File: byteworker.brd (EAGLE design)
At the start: 32 x 32 mm, 65 parts, among them IC1 MCP1703, IC2 TJA1043, J2 AVRSPI-61.27, Q1 BSS138, Q2 BSS138, Q3 BSS138, Q5 BSS138, Q6 FDN5618P, X1 16 MHz, X2 bus connector

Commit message: Done routing
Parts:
- removed Q6: FDN5618P, bytewerk-fet:SOT23C
- removed U$3, U$7, U$8: (no value), bytewerk-symbol:FIDUCIAL_R
- removed X2: bus connector, con-subd:F09D
- added D4: 16V, bytewerk-diode:SOD-128
- added Q4: AP2321GN-HF-3TR, bytewerk-transistor:SOT23-3
- added X3: SUBD-H9, bytewerk-con:SUBD9
- C2: value 10u/25v -> 1u/25V
- C3: value 10u/10v -> 1u/10V
- JP2: device pinhead:1X08 -> pinhead:1X06
- LED1: value n.b.[yellow] -> green
- LED2: value n.b.[green] -> blue
- LED3: value n.b.[red] -> red
- moved U$2 37.1 mm to (12.2, -0.71)
- moved U$4 35.5 mm to (12.0, -5.00), flipped to the bottom
- moved U$6 27.6 mm to (-13.2, 15.5)
- moved R8 23.4 mm to (12.5, 6.75), turned to 270 degrees
- moved R18 20.0 mm to (0.75, 11.5), flipped to the bottom, turned to 0 degrees
- moved J2 19.1 mm to (-9.75, 10.0), turned to 90 degrees
- moved TP2 18.5 mm to (12.5, 8.75)
- moved C1 18.3 mm to (-12.5, -6.25)
- moved U$5 17.8 mm to (8.25, 13.2), flipped to the top
- moved JP2 17.0 mm to (-1.35, -14.4)
- moved JP3 17.0 mm to (15.2, -3.02)
- moved C4 17.0 mm to (-5.00, -5.00)
- moved LED1 17.0 mm to (-3.75, -5.00)
- moved R17 17.0 mm to (4.75, 1.50)
- moved Q5 16.8 mm to (7.25, 0.75)
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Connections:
- net +5V: now also JP3.10; no longer JP2.3
- net CANH: now also X3.7; no longer X2.7
- net CANL: now also X3.2; no longer X2.2
- net GND: now also D4.A, JP2.6, X3.3; no longer JP2.8, JP3.10, X2.5
- net N$6: now also Q4.1; no longer Q6.1
- net OUT0: now also JP2.5; no longer JP2.7
- net OUT1: now also JP2.4; no longer JP2.6
- net OUT2: now also JP2.3; no longer JP2.5
- net VIN_BUS: now also X3.9; no longer X2.1
- net VIN_RECT: now also D4.C, Q4.2; no longer Q6.2
- net VOUT_SW: now also Q4.3; no longer Q6.3
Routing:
- net +5V: track 80.3 -> 122.7 mm, vias 4 -> 10
- net !CAN_STB!: track 26.9 -> 15.8 mm, vias 2 -> 3
- net SS_A/OC1B: track 51.3 -> 43.6 mm
- net !RESET!: track 13.7 -> 18.9 mm, vias 0 -> 2
- net MISO_A/OC1A: track 14.4 -> 19.5 mm
- net VIN_BUS: track 35.7 -> 31.1 mm
- net PB6: track 40.9 -> 36.5 mm
- net D2A: track 34.2 -> 37.9 mm
- net PD5/ADC2: track 16.5 -> 12.9 mm, vias 1 -> 2
- net VIN_RECT: track 53.3 -> 50.0 mm, vias 7 -> 5
- net OUT0: track 7.07 -> 9.80 mm
- net N$1: track 6.23 -> 8.85 mm
- net VIN_EXT: track 3.08 -> 5.62 mm
- net PC4: track 24.8 -> 27.3 mm
- net VOUT_SW: track 18.2 -> 20.1 mm
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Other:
- board size 32 x 32 mm -> 34 x 34 mm
- board text added: "v0.2.0"
- board text removed: "byte- Worker"
- board text removed: "v0.2"

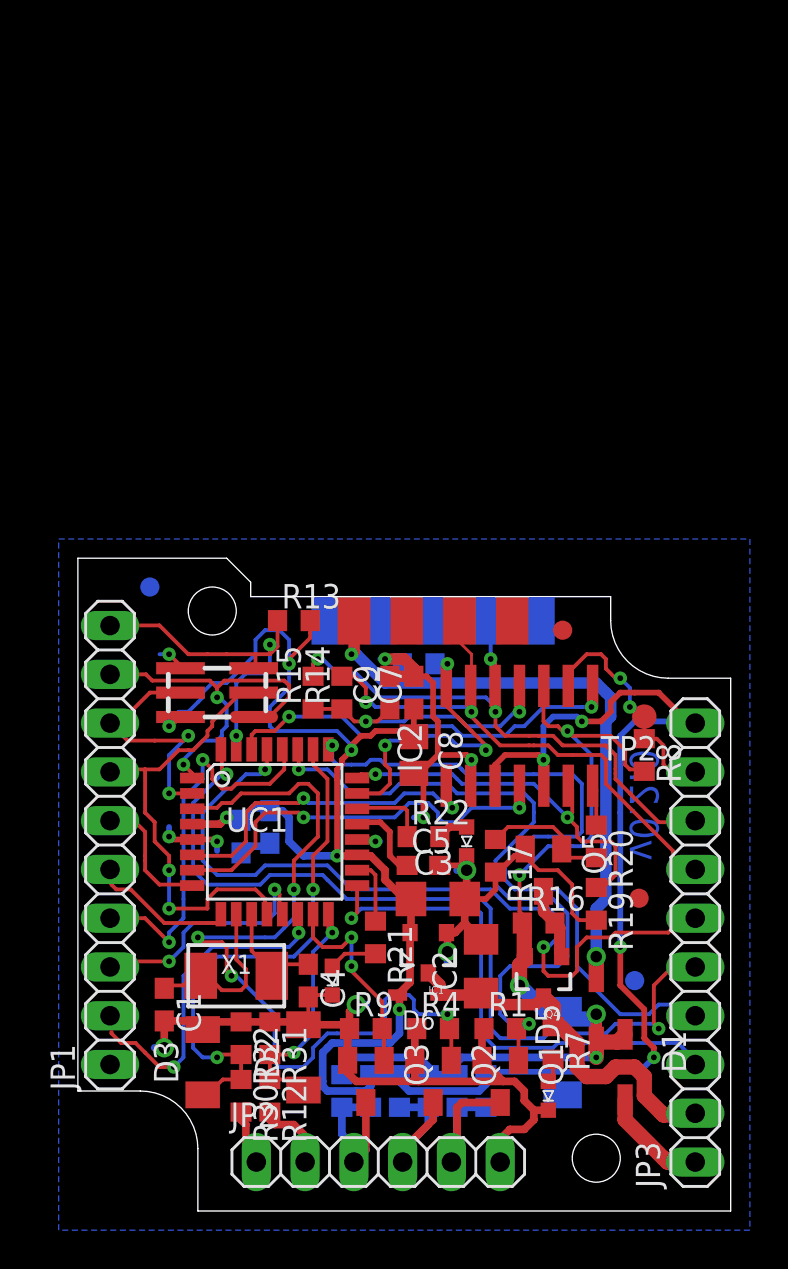
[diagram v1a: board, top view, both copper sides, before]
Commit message: v0.3.0: - swap subD connector for Male version. - center subD connector
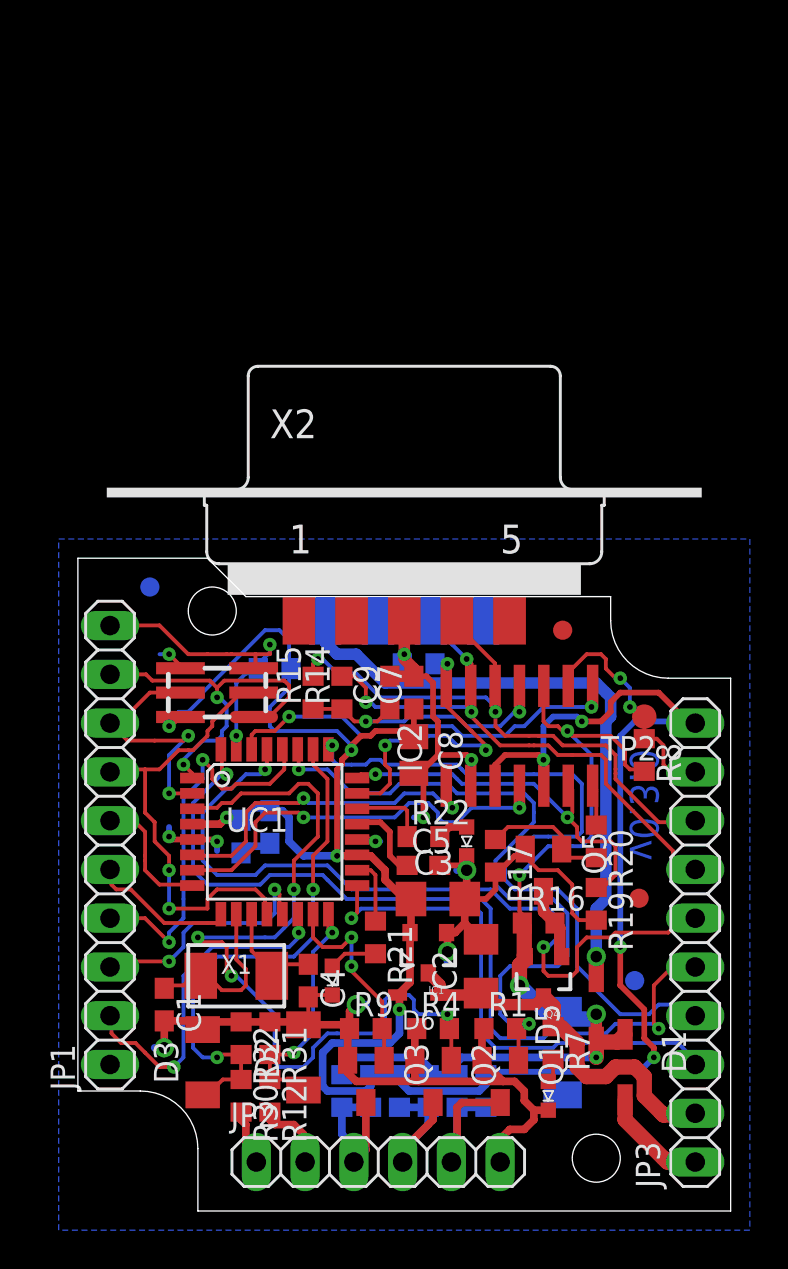
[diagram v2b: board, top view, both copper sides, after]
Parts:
- removed X3: SUBD-H9, bytewerk-con:SUBD9
- added X2: SUBD-M_H9, bytewerk-con:SUBD9
- moved R13 2.69 mm to (-6.75, 11.2), flipped to the bottom, turned to 180 degrees
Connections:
- net CANH: now also X2.8; no longer X3.7
- net CANL: now also X2.4; no longer X3.2
- net GND: now also X2.3; no longer X3.3
- net VIN_BUS: now also X2.6; no longer X3.9
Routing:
- net +5V: track 122.7 -> 118.6 mm, vias 10 -> 9
- net !RESET!: track 18.9 -> 16.6 mm
- net GND: track 87.8 -> 89.4 mm
- net VIN_BUS: track 31.1 -> 32.0 mm, vias 2 -> 1
- net CANL: track 30.5 -> 31.4 mm, vias 3 -> 2
- net CANH: track 29.4 -> 30.0 mm, vias 2 -> 3
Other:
- outline, holes or cut-outs redrawn
- board text added: "v0.3.0"
- board text removed: "v0.2.0"

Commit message: v0.4.0: - 500 mA +5V voltage regulator with larger package and input voltage - female sub-d connector - thicker power traces - removed 1 test-led
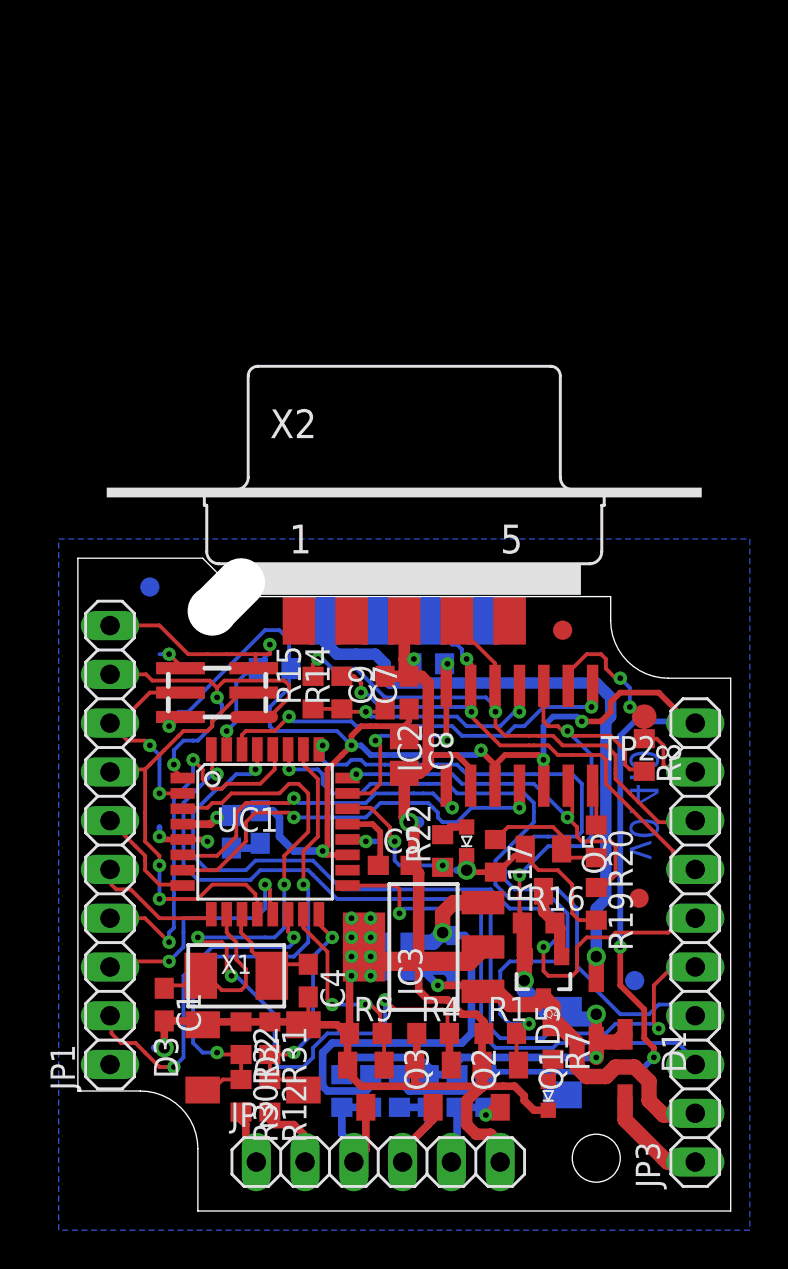
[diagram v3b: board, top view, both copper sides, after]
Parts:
- removed IC1: MCP1703, bytewerk-vreg:SOT23-3
- removed LED1: green, bytewerk-led:LED0603
- removed R21: 1k, bytewerk-passive:R0603
- added IC3: UA78M05IDCY, bytewerk-vreg:SOT223
- C2: value 1u/25V -> 100n; device bytewerk-rcl:C1206 -> bytewerk-passive:C0603
- C3: value 1u/10V -> 330n; device bytewerk-rcl:C1206 -> bytewerk-passive:C0603
- R7: value n.b.[1k] -> 1k
- moved C2 4.67 mm to (-0.50, -3.00), flipped to the bottom, turned to 0 degrees
- moved C3 4.37 mm to (-0.50, -4.50), flipped to the bottom
- moved D6 2.66 mm to (2.50, -3.75), flipped to the bottom, turned to 90 degrees
- moved C5 1.50 mm to (-0.50, 1.00)
- moved R22 1.25 mm to (2.00, 1.75), turned to 90 degrees
- moved C10 0.56 mm to (-9.00, 2.75)
- moved C6 0.50 mm to (-7.50, 3.00)
- moved C8 0.50 mm to (0.00, 6.75)
- moved R18 0.50 mm to (1.25, 11.5)
- moved UC1 0.50 mm to (-7.25, 2.75)
- moved C7 0.25 mm to (0.25, 10.0)
- moved C9 0.25 mm to (-1.00, 10.0)
- moved D3 0.25 mm to (-10.5, -9.00)
- moved Q1 0.25 mm to (5.00, -10.5)
- moved Q2 0.25 mm to (1.50, -10.5)
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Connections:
- removed net N$7: LED1.A, R21.2
- removed net TESTLED1: R21.1, UC1.18
- net +5V: now also C2.1, IC3.3; no longer C3.1, IC1.2
- net GND: now also IC3.2, IC3.4; no longer IC1.1, LED1.C
- net VOUT_SW: now also C3.1, IC3.1; no longer C2.1, IC1.3
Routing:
- net GND: track 89.4 -> 108.0 mm, vias 11 -> 16
- net +5V: track 118.6 -> 129.4 mm, vias 9 -> 10
- net OUT0: track 9.80 -> 5.79 mm, vias 0 -> 1
- net TESTLED1: track 3.46 -> 0.00 mm
- net !CAN_STB!: track 15.8 -> 12.4 mm
- net TESTLED2: track 4.04 -> 7.20 mm, vias 0 -> 2
- net VOUT_SW: track 20.1 -> 23.0 mm, vias 0 -> 1
- net TXD/MOSI_A/OC0A/SS: track 13.9 -> 11.2 mm
- net N$7: track 2.52 -> 0.00 mm
- net PB0/MISO: track 6.85 -> 5.63 mm
- net RXD/SCK_A: track 24.0 -> 23.0 mm
- net PB1/MOSI: track 7.75 -> 6.83 mm
- net N$4: track 14.8 -> 13.8 mm
- net AREF: track 4.31 -> 3.66 mm
- net PB6: track 36.5 -> 37.1 mm
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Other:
- outline, holes or cut-outs redrawn
- board text added: "v0.4.0"
- board text removed: "v0.3.0"

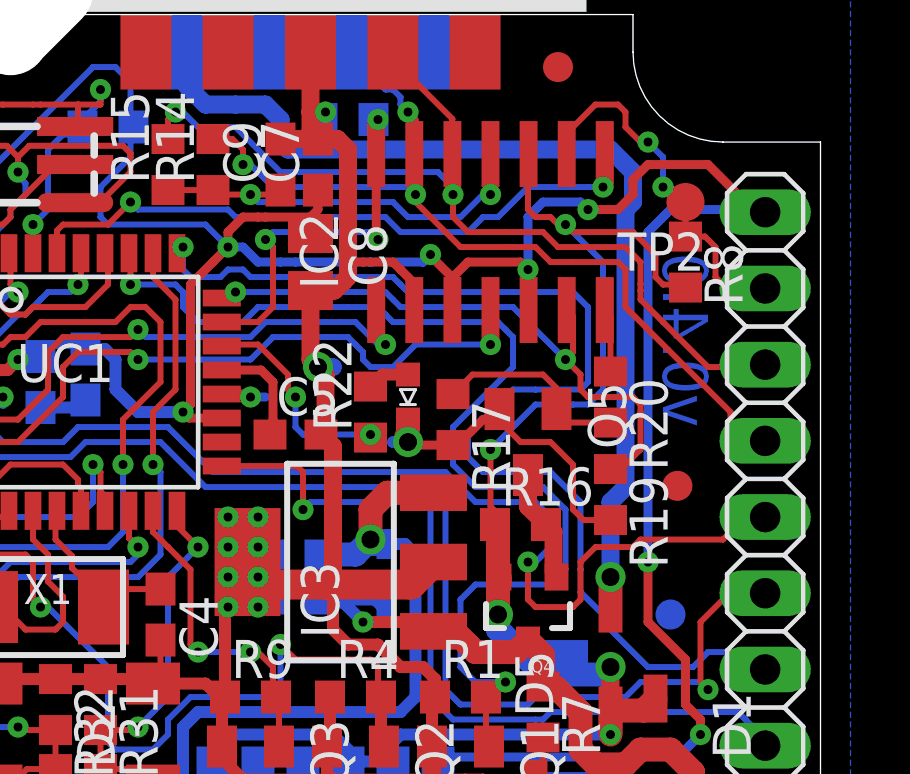
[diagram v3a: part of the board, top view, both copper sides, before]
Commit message: v4.1: add 2nd test LED
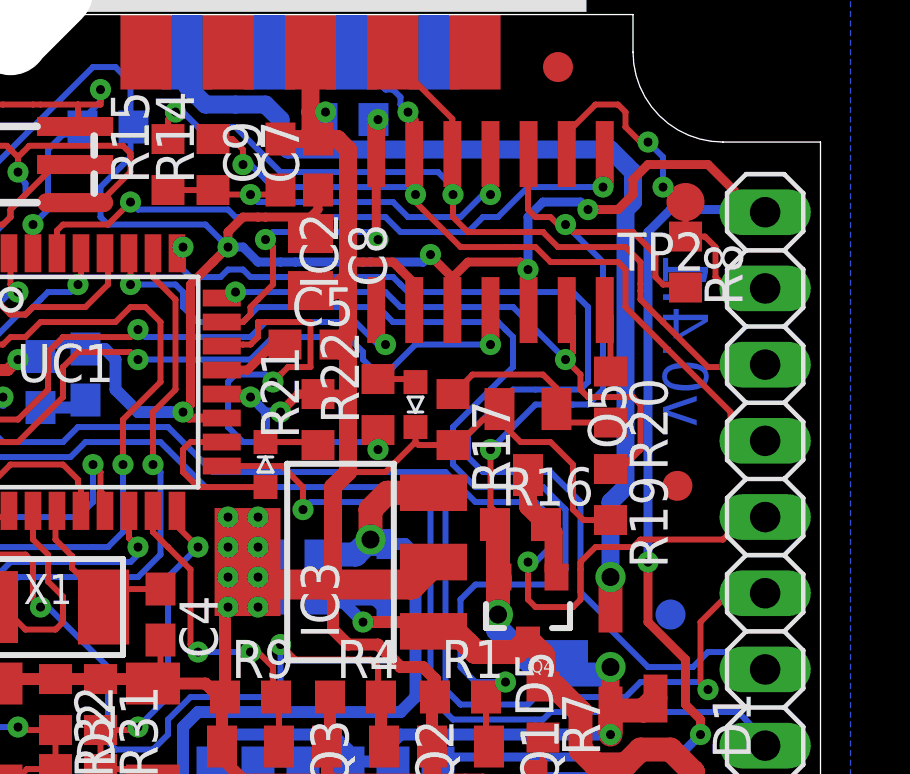
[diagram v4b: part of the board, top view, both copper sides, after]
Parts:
- added LED1: red, bytewerk-led:LED0603
- added R21: 1k, bytewerk-passive:R0603
- moved C5 3.04 mm to (0.00, 4.00)
- moved LED2 0.35 mm to (3.50, 2.00)
- moved R22 0.35 mm to (2.25, 2.00)
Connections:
- new net N$7: LED1.A, UC1.18
- new net N$9: LED1.C, R21.1
- net GND: now also R21.2
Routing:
- net TESTLED2: track 7.20 -> 15.7 mm
- net N$7: track 0.00 -> 5.10 mm
- net GND: track 108.0 -> 113.0 mm, vias 16 -> 15
- net N$9: track 0.00 -> 1.79 mm
- net AREF: track 3.66 -> 2.46 mm
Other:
- board text added: "v0.4.1"
- board text removed: "v0.4.0"
